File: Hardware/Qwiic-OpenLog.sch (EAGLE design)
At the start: 43 parts, among them J1 MICRO-SD, J10 GATORGATOR_MINI, J2 GATORGATOR_MINI, J3 GATORGATOR_MINI, J4 GATORGATOR_MINI, J5 ISP, J6 GATORGATOR_MINI, J7 GATORGATOR_MINI, J8 GATORGATOR_MINI, J9 GATORGATOR_MINI, Q1 16MHZ, Q2 2.5A/30V/105mΩ, U1 RV-1805, U2 ATMEGA328P

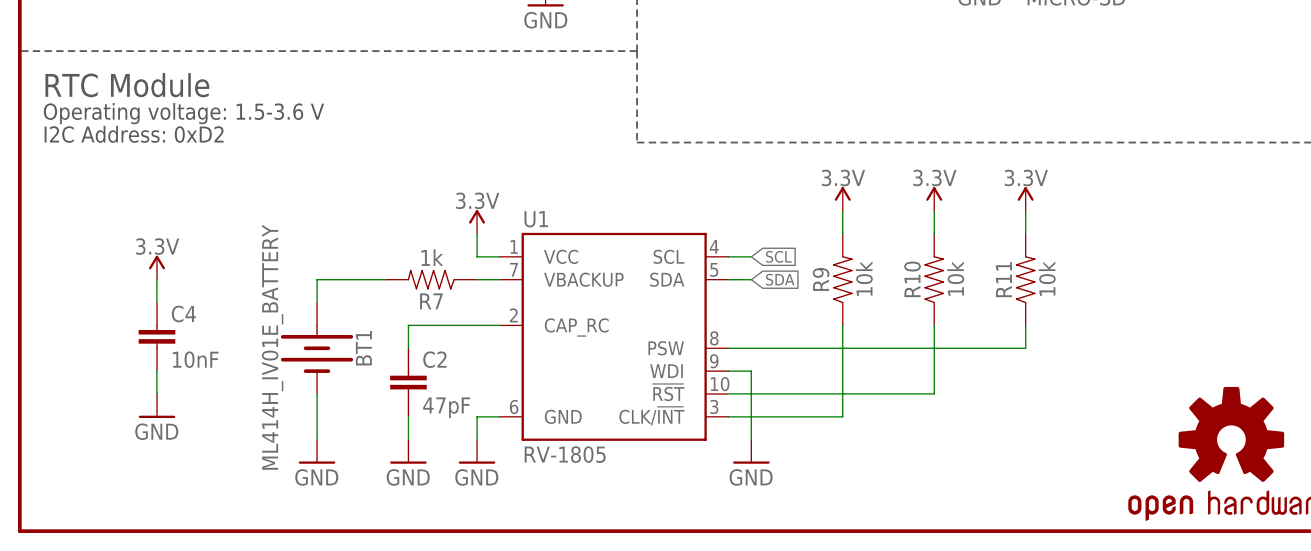
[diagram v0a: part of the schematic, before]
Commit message: updating to RV-3028
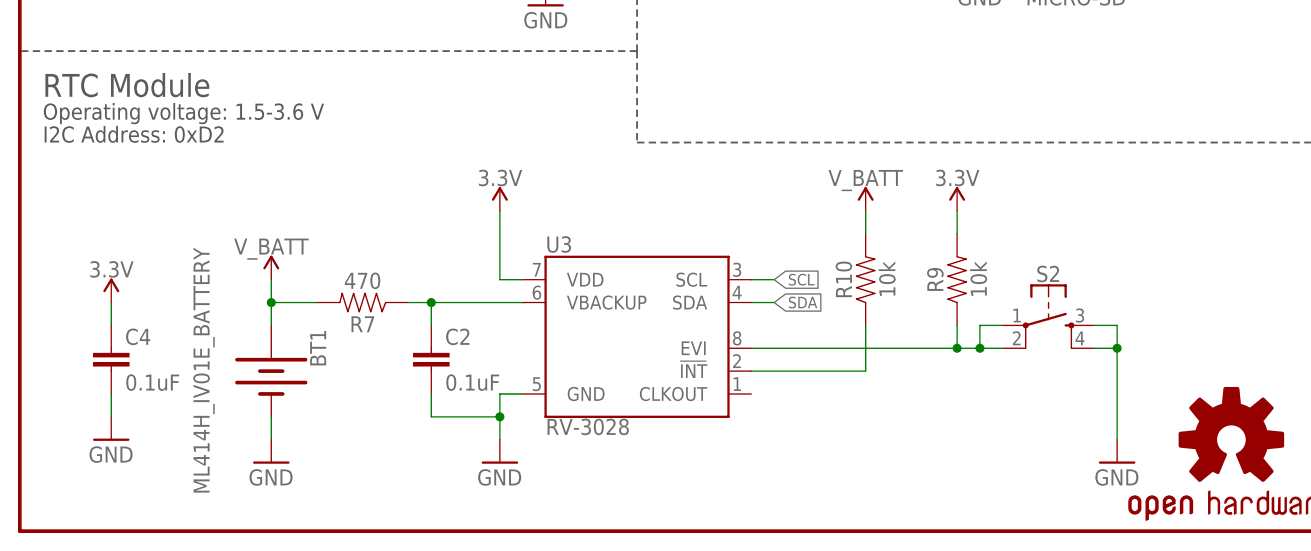
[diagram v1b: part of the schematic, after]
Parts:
- removed R11: 10k, SparkFun-Resistors:10KOHM-0603-1/10W-1%
- removed U1: RV-1805, SparkFun-Clocks:RV-1805
- added S2: (no value), SparkFun-Switches:MOMENTARY-SWITCH-SPST-2-SMD-5.2MM-TALL
- added U3: RV-3028, SparkFun-Clocks:RV-3028
- C2: value 47pF -> 0.1uF; device SparkFun-Capacitors:47PF-0603-50V-5% -> SparkFun-Capacitors:0.1UF-0603-25V-(+80/-20%)
- C4: value 10nF -> 0.1uF; device SparkFun-Capacitors:10NF-0603-50V-10% -> SparkFun-Capacitors:0.1UF-0603-25V-(+80/-20%)
- R7: value 1k -> 470; device SparkFun-Resistors:1KOHM-0603-1/10W-1% -> SparkFun-Resistors:470OHM-0603-1/10W-1%
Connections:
- removed net !INT: R9.1, U1.CLK/!INT
- removed net N$10: C2.1, U1.CAP_RC
- removed net PSW: R11.1, U1.PSW
- new net V_BATT: BT1.+, R10.2, R7.2
- net !RST: now also U3.!INT; no longer U1.!RST
- net 3.3V: now also U3.VDD; no longer R10.2, R11.2, U1.VCC
- net GND: now also S2.3, S2.4, U3.GND; no longer U1.GND, U1.WDI
- net N$8: now also R9.1, S2.1, S2.2, U3.EVI; no longer BT1.+, R7.2
- net SCL: now also U3.SCL; no longer U1.SCL
- net SDA: now also U3.SDA; no longer U1.SDA
- net VBACKUP: now also C2.1, U3.VBACKUP; no longer U1.VBACKUP
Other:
- moved on the sheet: BT1, C2, C4, R10, R7, R9

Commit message: pre reds review changes
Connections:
- removed net N$4: R1.1, U2.PD5(T1)
- net 3.3V: now also R1.1
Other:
- note added: "Input Voltage Range: 1.5-3.6 V"
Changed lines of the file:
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@@
 <?xml version="1.0" encoding="utf-8"?>
 <!DOCTYPE eagle SYSTEM "eagle.dtd">
-<eagle version="9.1.0">
+<eagle version="9.1.2">
 <drawing>
 <settings>
@@
 <part name="GND10" library="SparkFun" deviceset="GND" device=""/>
 <part name="S2" library="SparkFun-Switches" deviceset="MOMENTARY-SWITCH-SPST-2" device="-SMD-5.2MM-TALL"/>
+<part name="P+4" library="SparkFun" deviceset="3.3V" device=""/>
 </parts>
 <sheets>
@@
 <text x="238.76" y="7.62" size="2.54" layer="94" font="vector">v01</text>
 <text x="167.894" y="11.43" size="2.54" layer="94" font="vector">A. England</text>
-<text x="17.78" y="170.18" size="2.54" layer="97" font="vector">I2C Pull-up</text>
-<text x="20.32" y="109.22" size="2.54" layer="97" font="vector">Communication</text>
-<text x="93.98" y="109.22" size="2.54" layer="97" font="vector">MicroSD Socket</text>
-<text x="91.44" y="170.18" size="2.54" layer="97" font="vector">ISP Header</text>
+<text x="2.54" y="180.34" size="2.54" layer="97" font="vector">I2C Pull-up</text>
+<text x="2.54" y="109.22" size="2.54" layer="97" font="vector">Communication</text>
+<text x="71.12" y="109.22" size="2.54" layer="97" font="vector">MicroSD Socket</text>
+<text x="71.12" y="180.34" size="2.54" layer="97" font="vector">ISP Header</text>
 <wire x1="68.58" y1="53.34" x2="0" y2="53.34" width="0.2032" layer="97" style="shortdash"/>
 <wire x1="147.32" y1="43.18" x2="147.32" y2="114.3" width="0.2032" layer="97" style="shortdash"/>
@@
 <wire x1="68.58" y1="43.18" x2="147.32" y2="43.18" width="0.2032" layer="97" style="shortdash"/>
 <wire x1="147.32" y1="43.18" x2="147.32" y2="35.56" width="0.2032" layer="97" style="shortdash"/>
-<text x="185.42" y="172.72" size="2.54" layer="97" font="vector">ATMEGA328</text>
-<text x="185.42" y="170.18" size="1.778" layer="97" font="vector">Operating voltage: 1.5-3.6 V</text>
+<text x="149.86" y="180.34" size="2.54" layer="97" font="vector">ATMEGA328</text>
+<text x="149.86" y="177.8" size="1.778" layer="97" font="vector">Operating voltage: 1.5-3.6 V</text>
+<text x="2.54" y="106.68" size="1.778" layer="97" font="vector">Input Voltage Range: 1.5-3.6 V</text>
 </plain>
 <instances>
@@
 </instance>
 <instance part="S2" gate="G$1" x="114.3" y="22.86"/>
+<instance part="P+4" gate="G$1" x="236.22" y="91.44" smashed="yes">
+<attribute name="VALUE" x="235.204" y="94.996" size="1.778" layer="96" font="vector"/>
+</instance>
 </instances>
 <busses>
@@
 </segment>
 </net>
-<net name="N$4" class="0">
-<segment>
-<wire x1="220.98" y1="111.76" x2="236.22" y2="111.76" width="0.1524" layer="91"/>
-<wire x1="236.22" y1="111.76" x2="236.22" y2="86.36" width="0.1524" layer="91"/>
-<pinref part="R1" gate="G$1" pin="1"/>
-<pinref part="U2" gate="U1" pin="PD5(T1)"/>
-</segment>
-</net>
 <net name="3.3V" class="0">
 <segment>
@@
 <wire x1="104.14" y1="35.56" x2="104.14" y2="33.02" width="0.1524" layer="91"/>
 </segment>
-</net>
+<segment>
+<wire x1="236.22" y1="91.44" x2="236.22" y2="86.36" width="0.1524" layer="91"/>
+<pinref part="R1" gate="G$1" pin="1"/>
+<pinref part="P+4" gate="G$1" pin="3.3V"/>
+</segment>
+</net>

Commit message: engineer run of checklist
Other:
- note added: "7-bit Unshifted I2C Address: 0xA4"
- note added: "v10"
- note removed: "I2C Address: 0xD2"
- note removed: "v01"
- moved on the sheet: D2, D4, D5, J10, J2, J3, J4, J6, J7, J8, J9, Q2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
